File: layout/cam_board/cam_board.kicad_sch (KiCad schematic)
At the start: 80 parts, among them J1 Stick conn, J2 LCD conn, J3 Conn_01x05_Pin, J4 USB Connector, J5 BATT_CONNECTOR, SW1 BOOT0, SW2 USER, SW3 NRST, SW4 ON/OFF, U1 W25Q128JVS, U2 STM32F401CCUx, U3 AP2112K-3.3, U4 MCP73871-1AA, U5 USBLC6-2SC6, Y1 SC32S-7PF20PPM, Y2 ECS-80-18-23B-JTN-TR

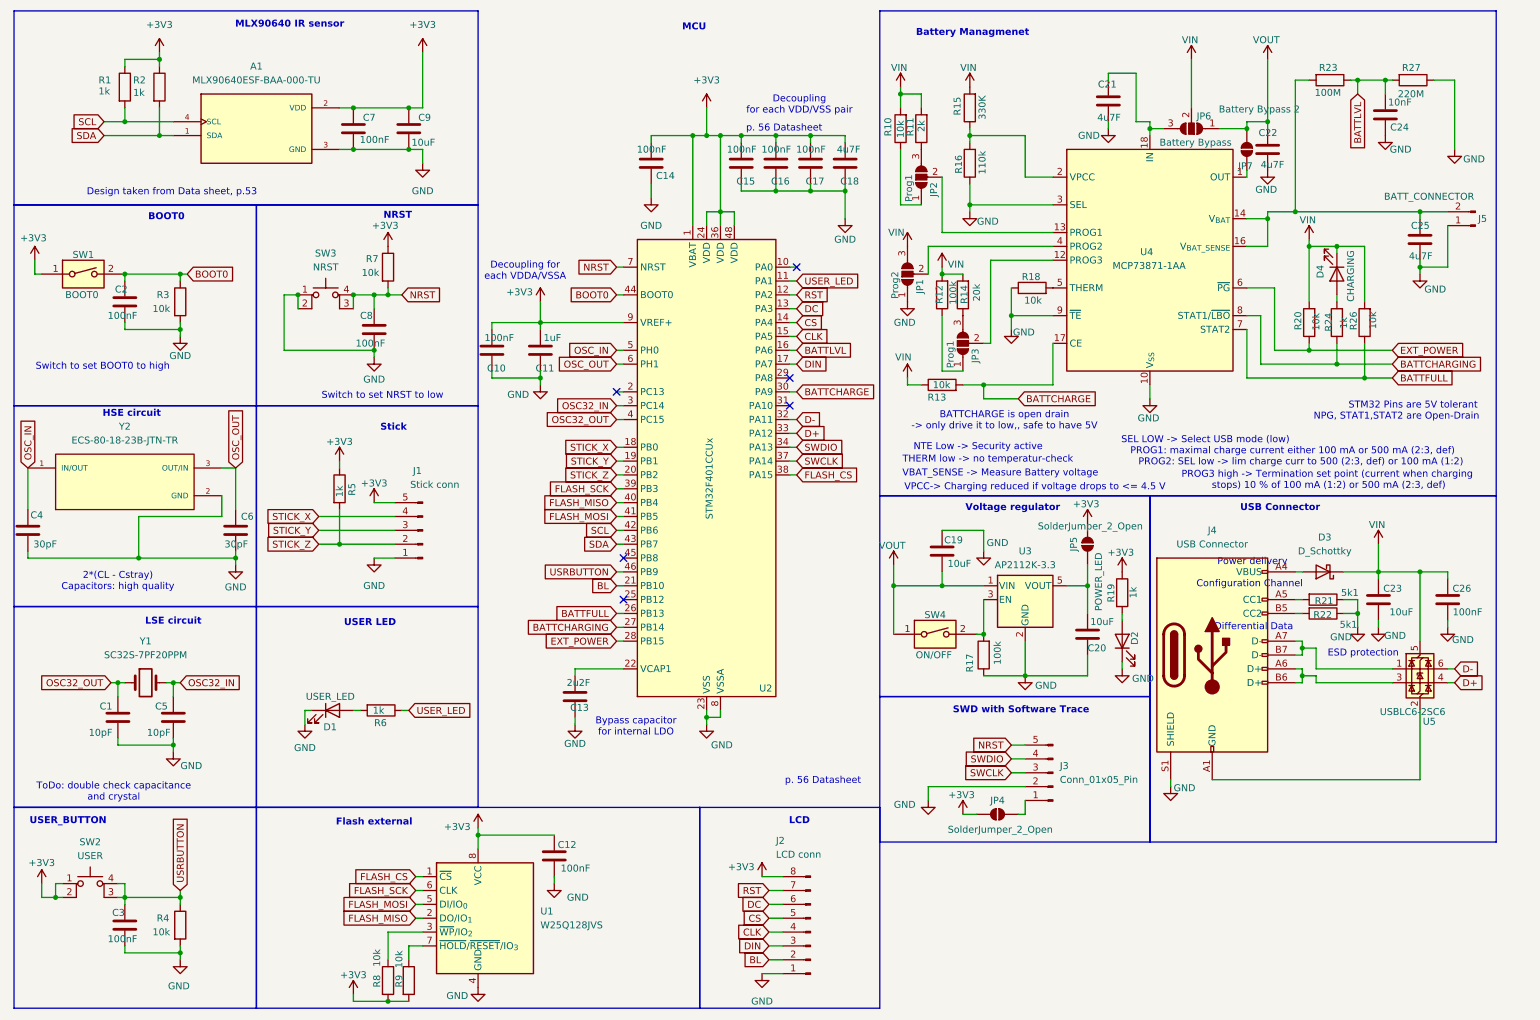
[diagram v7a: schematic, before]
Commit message: Add optional USB pullup, add more LEDs
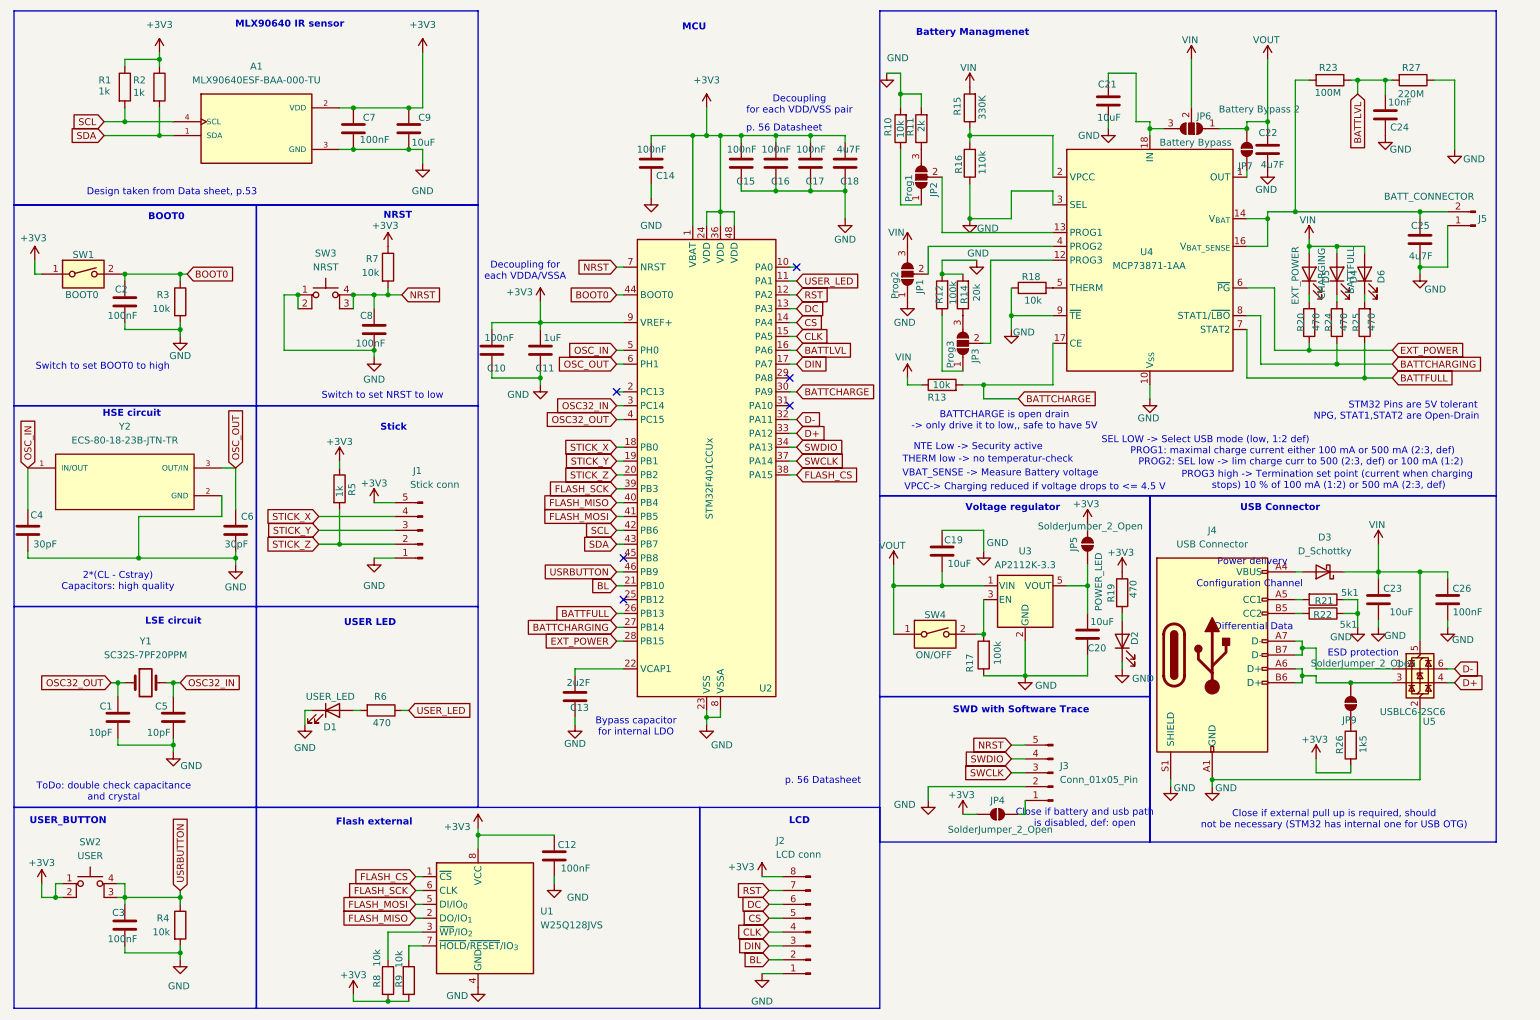
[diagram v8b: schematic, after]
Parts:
- added D5: EXT_POWER, LED_SMD:LED_0603_1608Metric_Pad1.05x0.95mm_HandSolder, symbol Device:LED
- added D6: BATTFULL, LED_SMD:LED_0603_1608Metric_Pad1.05x0.95mm_HandSolder, symbol Device:LED
- added JP9: SolderJumper_2_Open, Jumper:SolderJumper-2_P1.3mm_Open_RoundedPad1.0x1.5mm, symbol Jumper:SolderJumper_2_Open
- added R25: 470, Resistor_SMD:R_0603_1608Metric_Pad0.98x0.95mm_HandSolder, symbol Device:R
- C21: value 4u7F -> 10uF
- JP3: value Prog1 -> Prog3
- R19, R24, R6: value 1k -> 470
- R20: value 10k -> 470
- R26: value 10k -> 1k5
- SW4: footprint Button_Switch_SMD:SW_DIP_SPSTx01_Slide_6.7x4.1mm_W8.61mm_P2.54mm_LowProfile -> Button_Switch_THT:SW_DIP_SPSTx01_Slide_9.78x4.72mm_W7.62mm_P2.54mm
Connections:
- net +3V3: now also R26.1
- net BATTFULL: now also R25.1; no longer R26.1
- net GND: now also J4.A1 (GND), J4.A12 (GND), J4.B1 (GND), J4.B12 (GND), R10.2, R11.2, R12.2, R14.2, U5.2 (GND)
- net VIN: now also D4.2 (A), D5.2 (A), D6.2 (A); no longer D4.1 (K), R10.2, R11.2, R12.2, R14.2, R20.2, R26.2
- net at R24.2: now also D4.1 (K); no longer D4.2 (A)
- net at J4.A6 (D+), J4.B6 (D+), U5.3 (I/O2): now also JP9.2 (B)
- new net: D5.1 (K), R20.2
- new net: D6.1 (K), R25.2
- new net: JP9.1 (A), R26.2
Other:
- note added: "Close if battery and usb path is disabled, def: open"
- note added: "Close if external pull up is required, should not be necessary (STM32 has internal one for USB OTG)"
- note added: "SEL LOW -> Select USB mode (low, 1:2 def)"
- note removed: "SEL LOW -> Select USB mode (low)"
- moved on the sheet: D4
